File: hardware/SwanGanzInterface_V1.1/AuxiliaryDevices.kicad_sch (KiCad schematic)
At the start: 19 parts, among them IC1 TSC2046IPWR, J8 1051640001, U6 FT232RL

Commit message: Added lots, moving to 64 pin micro
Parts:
- added C32: 0.1u, symbol Device:C
- added R1, R2: R, symbol Device:R
- added TP21: TOUCH_CS3, SGI_FootprintsLib:Testpoint_1x02_P2.54mm, symbol SGI_SymbolLib:Testpoint
- added TP22: TOUCH_SCK, SGI_FootprintsLib:Testpoint_1x02_P2.54mm, symbol SGI_SymbolLib:Testpoint
- added TP23: TOUCH_PICO, SGI_FootprintsLib:Testpoint_1x02_P2.54mm, symbol SGI_SymbolLib:Testpoint
- added TP24: TOUCH_BUSY, SGI_FootprintsLib:Testpoint_1x02_P2.54mm, symbol SGI_SymbolLib:Testpoint
- added TP25: TOUCH_POCI, SGI_FootprintsLib:Testpoint_1x02_P2.54mm, symbol SGI_SymbolLib:Testpoint
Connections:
- net +3V3: now also C32.1
- net GND: now also C32.2, R2.2
- net TOUCH_SPI0_CS3: now also TP21.1 (A), TP21.2 (B)
- net TOUCH_SPI0_PICO: now also TP23.1 (A), TP23.2 (B)
- net TOUCH_SPI0_POCI: now also TP25.1 (A), TP25.2 (B)
- net TOUCH_SPI0_SCK: now also TP22.1 (A), TP22.2 (B)
- net TouchBusy: now also TP24.1 (A), TP24.2 (B)
- net MICRO_VBUS: now reaches J8.1 (VBUS), JP1.2 (B)
- net MICRO_VBUS: now also R1.1
- net USB_CBUS2: no longer names the net of U6.13 (CBUS2)
- net USB_CBUS3: no longer names the net of U6.14 (CBUS3)
- new net USB_CONN_PA10: R1.2, R2.1
- no-connect marks 11 -> 13
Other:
- note added: "Data Sheet says to have caps on D+/D- This seems stupid though"
- note added: "Need Ferrite Bead?"
- note added: "Resistor Values"
- note added: "VCC = 5V to power internal 3V3 LDO VCCIO = 3V3 to set UART to 3V3 logic"
- moved on the sheet: JP1

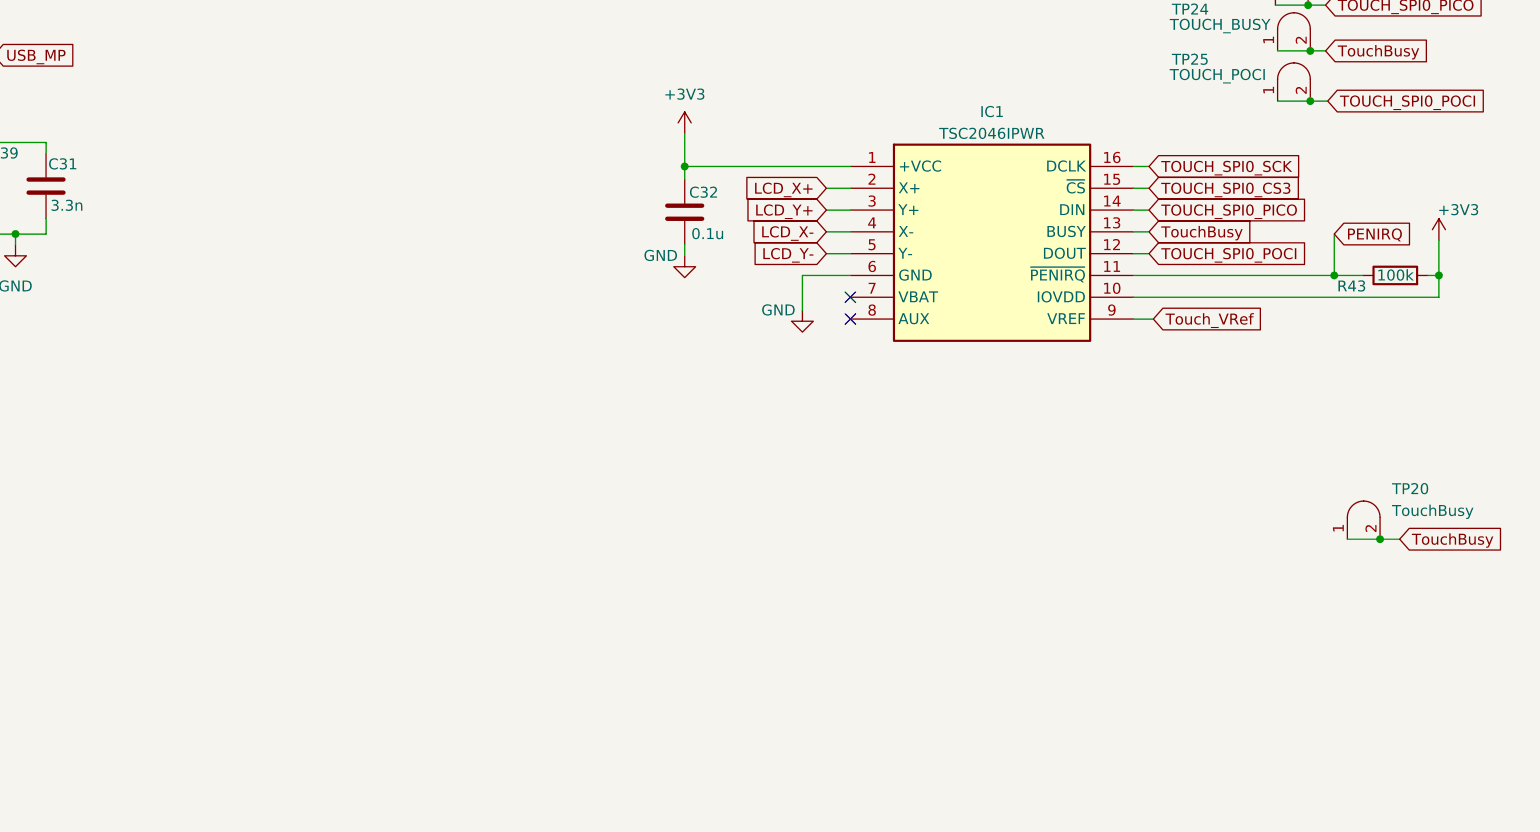
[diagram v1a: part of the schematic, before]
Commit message: Got 64 pin MSP symbol and footprint and started implementation
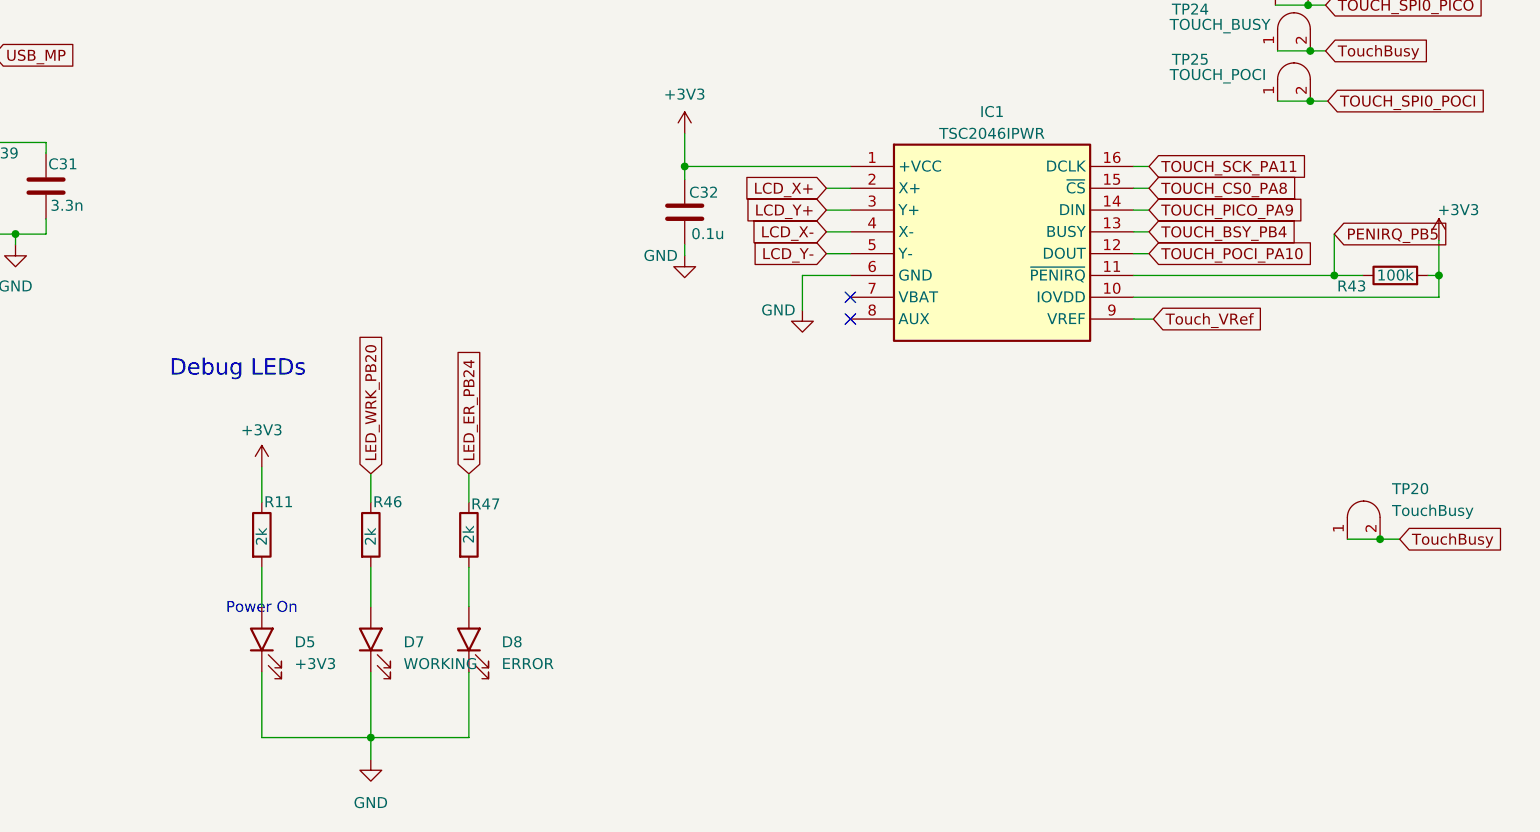
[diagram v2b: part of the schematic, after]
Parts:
- added D5: +3V3, SGI_FootprintsLib:LED_D5.0mm, symbol SGI_SymbolLib:LED
- added D7: WORKING, SGI_FootprintsLib:LED_D5.0mm, symbol SGI_SymbolLib:LED
- added D8: ERROR, SGI_FootprintsLib:LED_D5.0mm, symbol SGI_SymbolLib:LED
- added R11, R46, R47: 2k, Resistor_SMD:R_0603_1608Metric, symbol Device:R
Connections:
- net +3V3: now also R11.1
- net GND: now also D5.1 (K), D7.1 (K), D8.1 (K)
- net TOUCH_SPI0_CS3: no longer IC1.15 (~{CS})
- net TOUCH_SPI0_PICO: no longer IC1.14 (DIN)
- net TOUCH_SPI0_POCI: no longer IC1.12 (DOUT)
- net TOUCH_SPI0_SCK: no longer IC1.16 (DCLK)
- net TouchBusy: no longer IC1.13 (BUSY)
- net PENIRQ renamed PENIRQ_PB5
- new net: D7.2 (A), R46.2
- new net: D8.2 (A), R47.2
- new net: D5.2 (A), R11.2
- new net LED_ER_PB24: R47.1
- new net LED_WRK_PB20: R46.1
- new net TOUCH_BSY_PB4: IC1.13 (BUSY)
- new net TOUCH_CS0_PA8: IC1.15 (~{CS})
- new net TOUCH_PICO_PA9: IC1.14 (DIN)
- new net TOUCH_POCI_PA10: IC1.12 (DOUT)
- new net TOUCH_SCK_PA11: IC1.16 (DCLK)
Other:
- note added: "Debug LEDs"
- note added: "Power On"

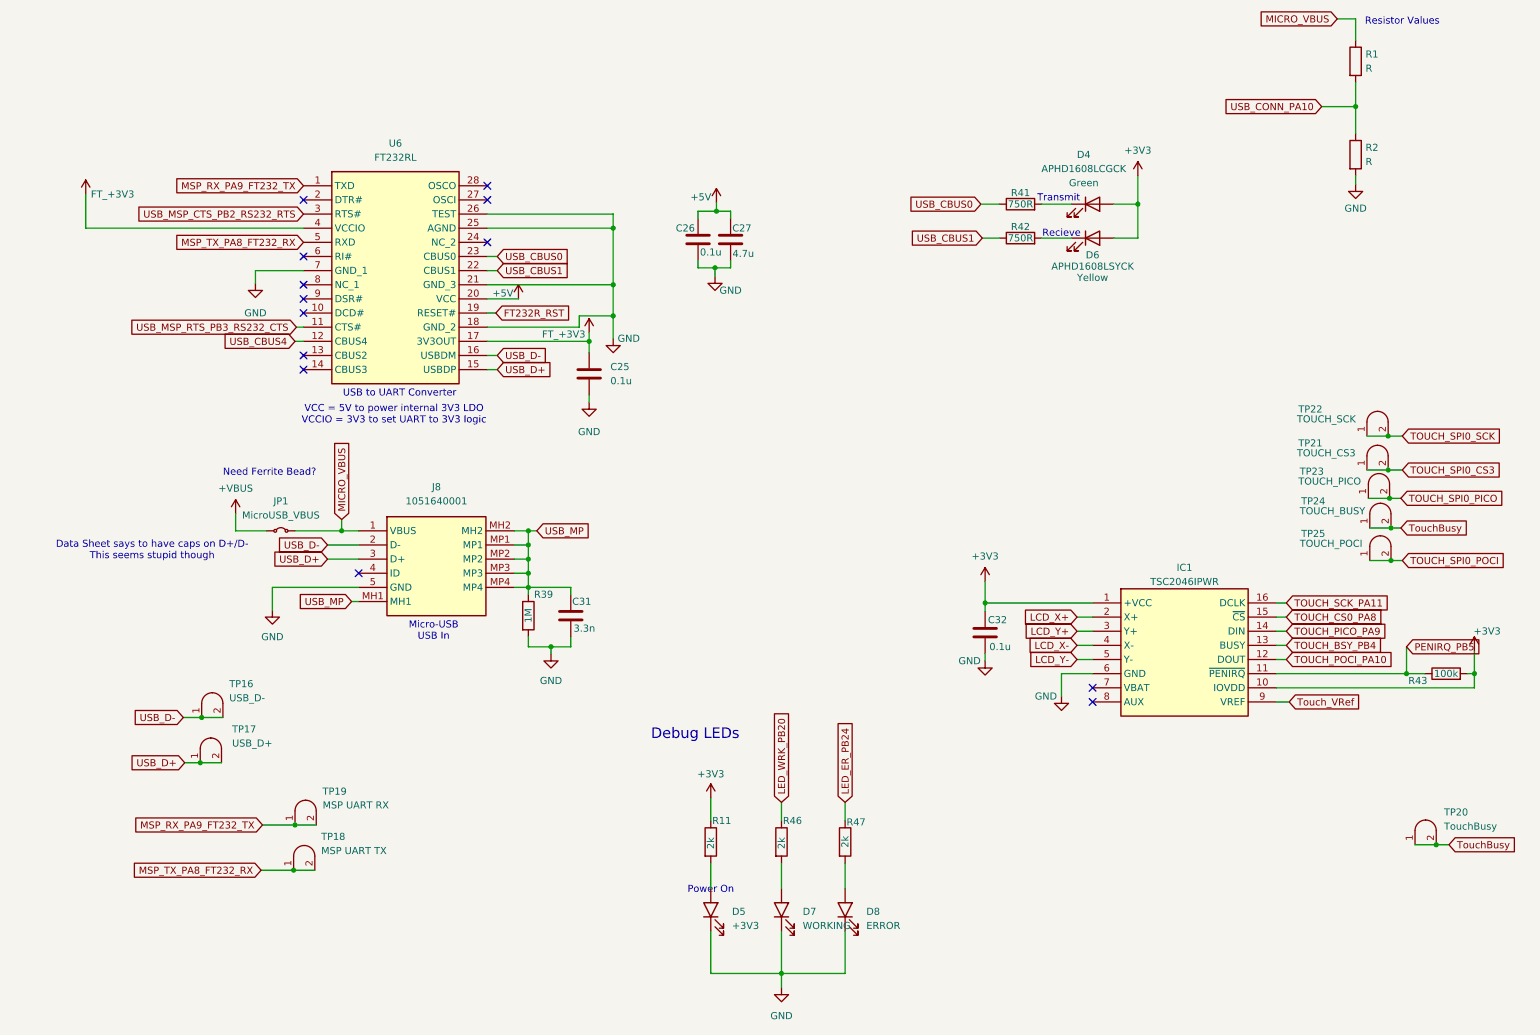
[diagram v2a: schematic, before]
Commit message: Added debug pins to touch ic and ft232
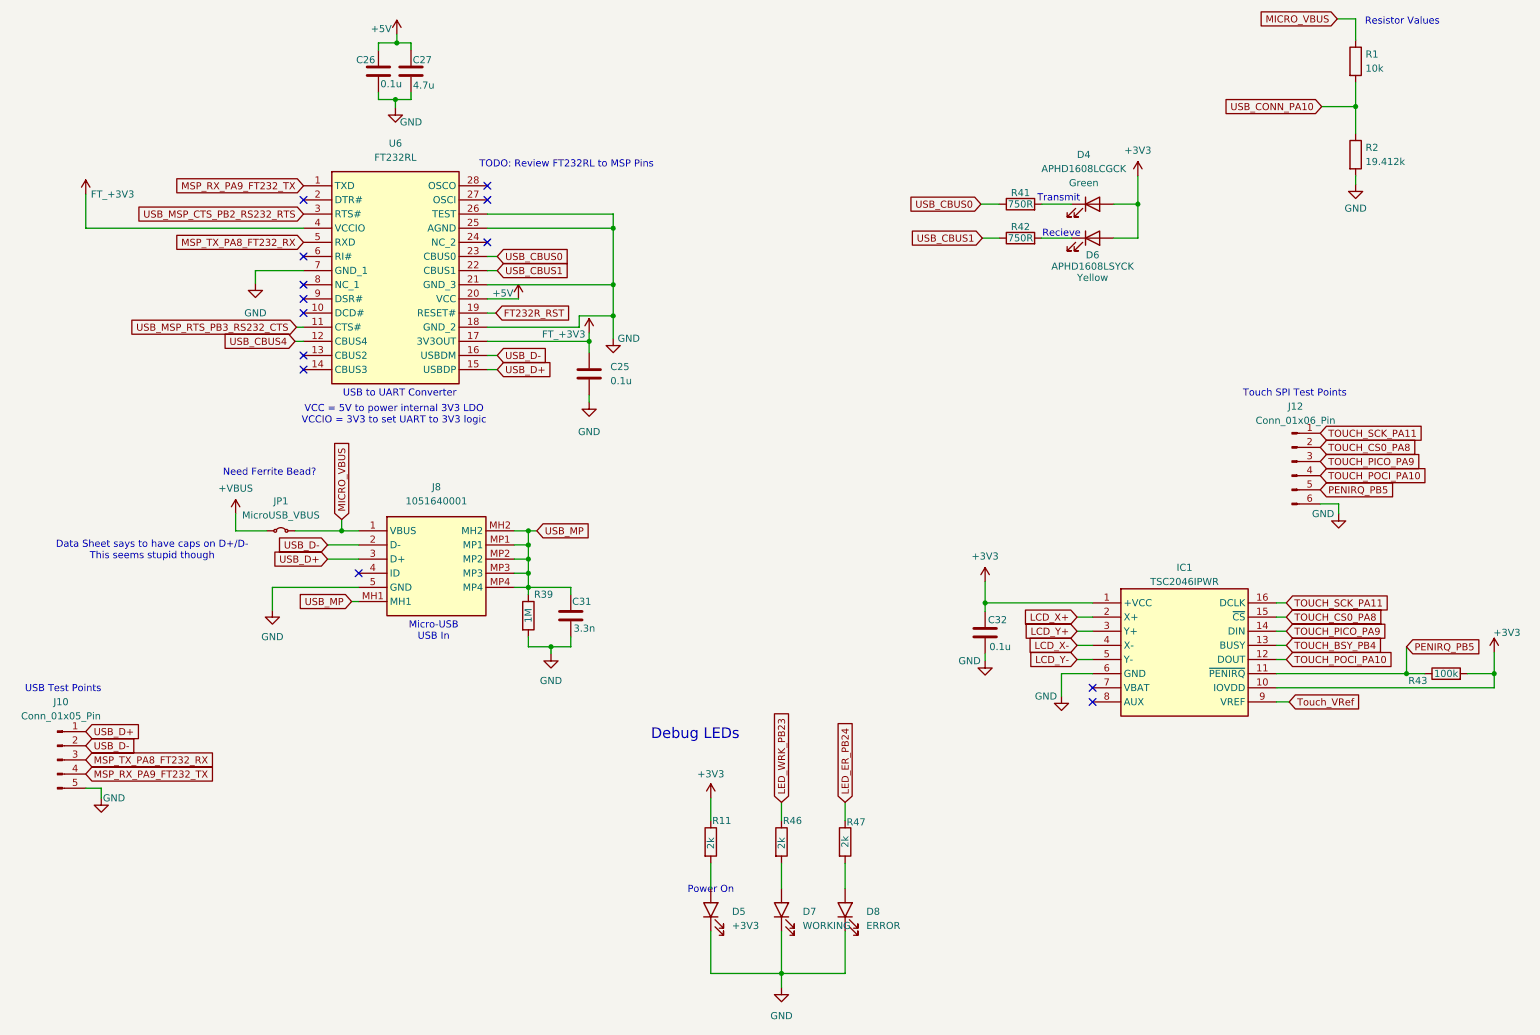
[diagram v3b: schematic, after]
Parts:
- removed TP16: USB_D-, SGI_FootprintsLib:Testpoint_1x02_P2.54mm, symbol SGI_SymbolLib:Testpoint
- removed TP17: USB_D+, SGI_FootprintsLib:Testpoint_1x02_P2.54mm, symbol SGI_SymbolLib:Testpoint
- removed TP18: MSP UART TX, SGI_FootprintsLib:Testpoint_1x02_P2.54mm, symbol SGI_SymbolLib:Testpoint
- removed TP19: MSP UART RX, SGI_FootprintsLib:Testpoint_1x02_P2.54mm, symbol SGI_SymbolLib:Testpoint
- removed TP20: TouchBusy, SGI_FootprintsLib:Testpoint_1x02_P2.54mm, symbol SGI_SymbolLib:Testpoint
- removed TP21: TOUCH_CS3, SGI_FootprintsLib:Testpoint_1x02_P2.54mm, symbol SGI_SymbolLib:Testpoint
- removed TP22: TOUCH_SCK, SGI_FootprintsLib:Testpoint_1x02_P2.54mm, symbol SGI_SymbolLib:Testpoint
- removed TP23: TOUCH_PICO, SGI_FootprintsLib:Testpoint_1x02_P2.54mm, symbol SGI_SymbolLib:Testpoint
- removed TP24: TOUCH_BUSY, SGI_FootprintsLib:Testpoint_1x02_P2.54mm, symbol SGI_SymbolLib:Testpoint
- removed TP25: TOUCH_POCI, SGI_FootprintsLib:Testpoint_1x02_P2.54mm, symbol SGI_SymbolLib:Testpoint
- added J10: Conn_01x05_Pin, symbol Connector:Conn_01x05_Pin
- added J12: Conn_01x06_Pin, symbol Connector:Conn_01x06_Pin
- R1: value R -> 10k
- R2: value R -> 19.412k
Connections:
- net GND: now also J10.5 (Pin_5), J12.6 (Pin_6)
- net MSP_RX_PA9_FT232_TX: now also J10.4 (Pin_4)
- net MSP_TX_PA8_FT232_RX: now also J10.3 (Pin_3)
- net PENIRQ_PB5: now also J12.5 (Pin_5)
- net TOUCH_CS0_PA8: now also J12.2 (Pin_2)
- net TOUCH_PICO_PA9: now also J12.3 (Pin_3)
- net TOUCH_POCI_PA10: now also J12.4 (Pin_4)
- net TOUCH_SCK_PA11: now also J12.1 (Pin_1)
- net USB_D+: now also J10.1 (Pin_1)
- net USB_D-: now also J10.2 (Pin_2)
- net LED_WRK_PB20 renamed LED_WRK_PB23
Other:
- note added: "TODO: Review FT232RL to MSP Pins"
- note added: "Touch SPI Test Points"
- note added: "USB Test Points"
- moved on the sheet: C26, C27

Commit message: LCD spi debugging pins
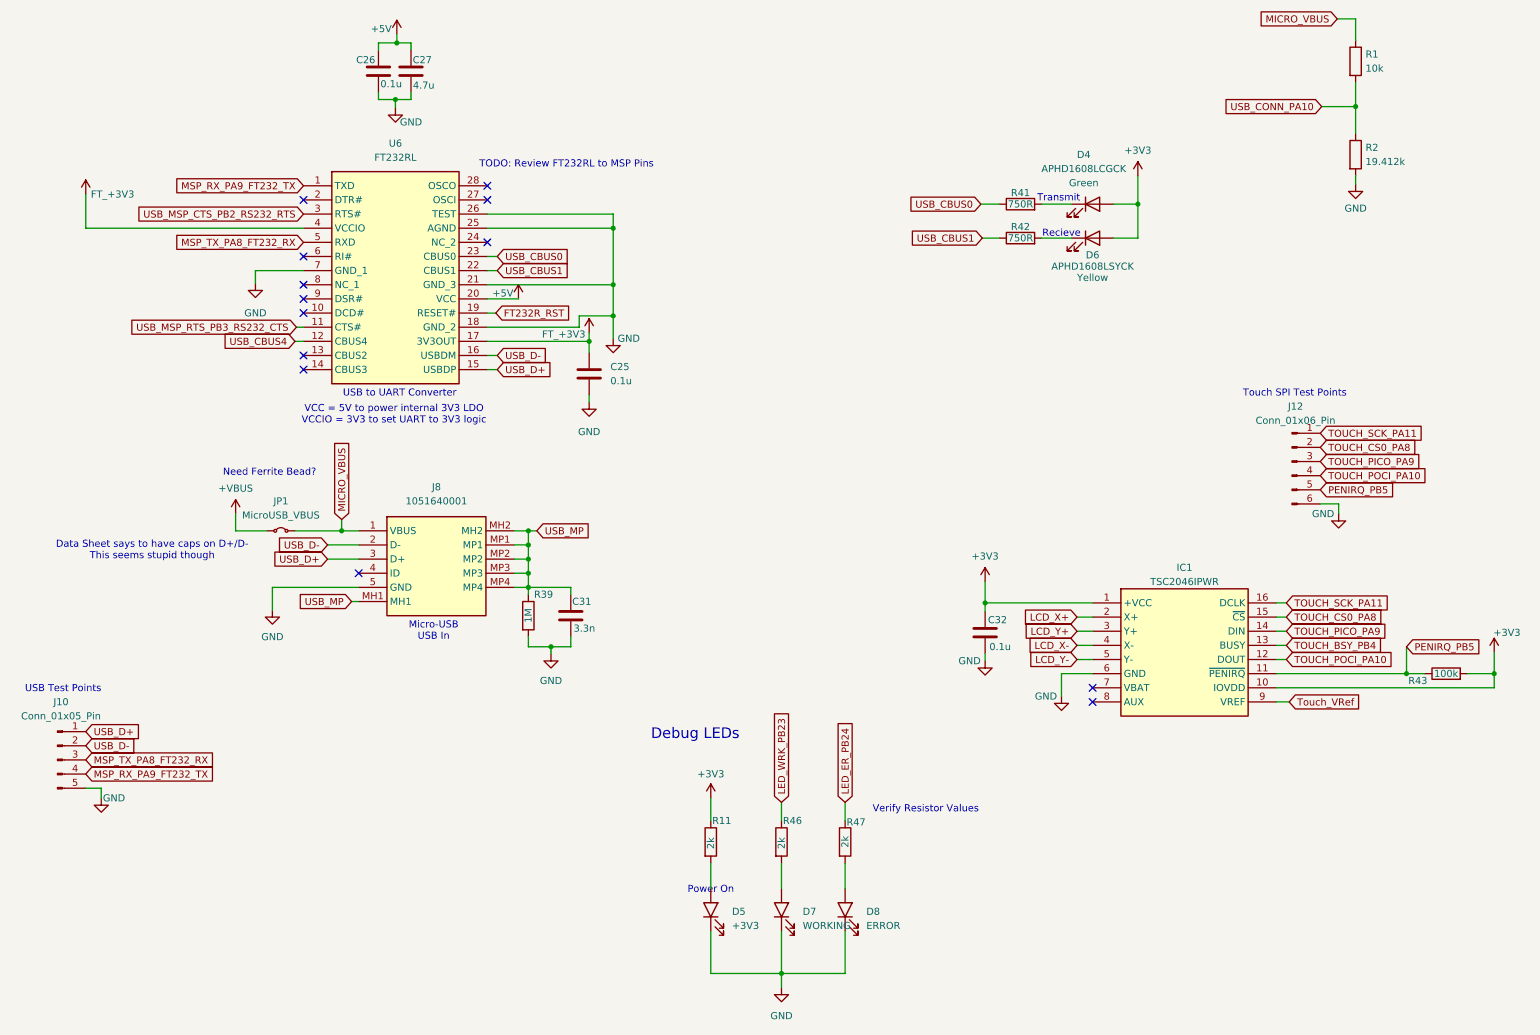
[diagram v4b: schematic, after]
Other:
- note added: "Verify Resistor Values"
- note removed: "Resistor Values"
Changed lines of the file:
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@@
 		(comment 1 "Senior Design Project Fall 2025 - Spring 2026")
-	)
-	(text "Resistor Values"
-		(exclude_from_sim no)
-		(at 263.144 14.986 0)
-		(effects
-			(font
-				(size 1.27 1.27)
-			)
-		)
 	)
 	(text "TODO: Review FT232RL to MSP Pins"
@@
 		(effects
 			(font
+				(size 1.27 1.27)
+			)
+		)
+	)
+	(text "Verify Resistor Values"
+		(exclude_from_sim no)
+		(at 177.546 156.464 0)
+		(effects
+			(font
